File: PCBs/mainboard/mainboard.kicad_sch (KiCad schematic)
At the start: 26 parts, among them J1 USB_C_Receptacle_USB2.0_16P, SW1 SW_Push_Dual, SW2 SW_Push_Dual, U3 ESP32-S3-WROOM-1

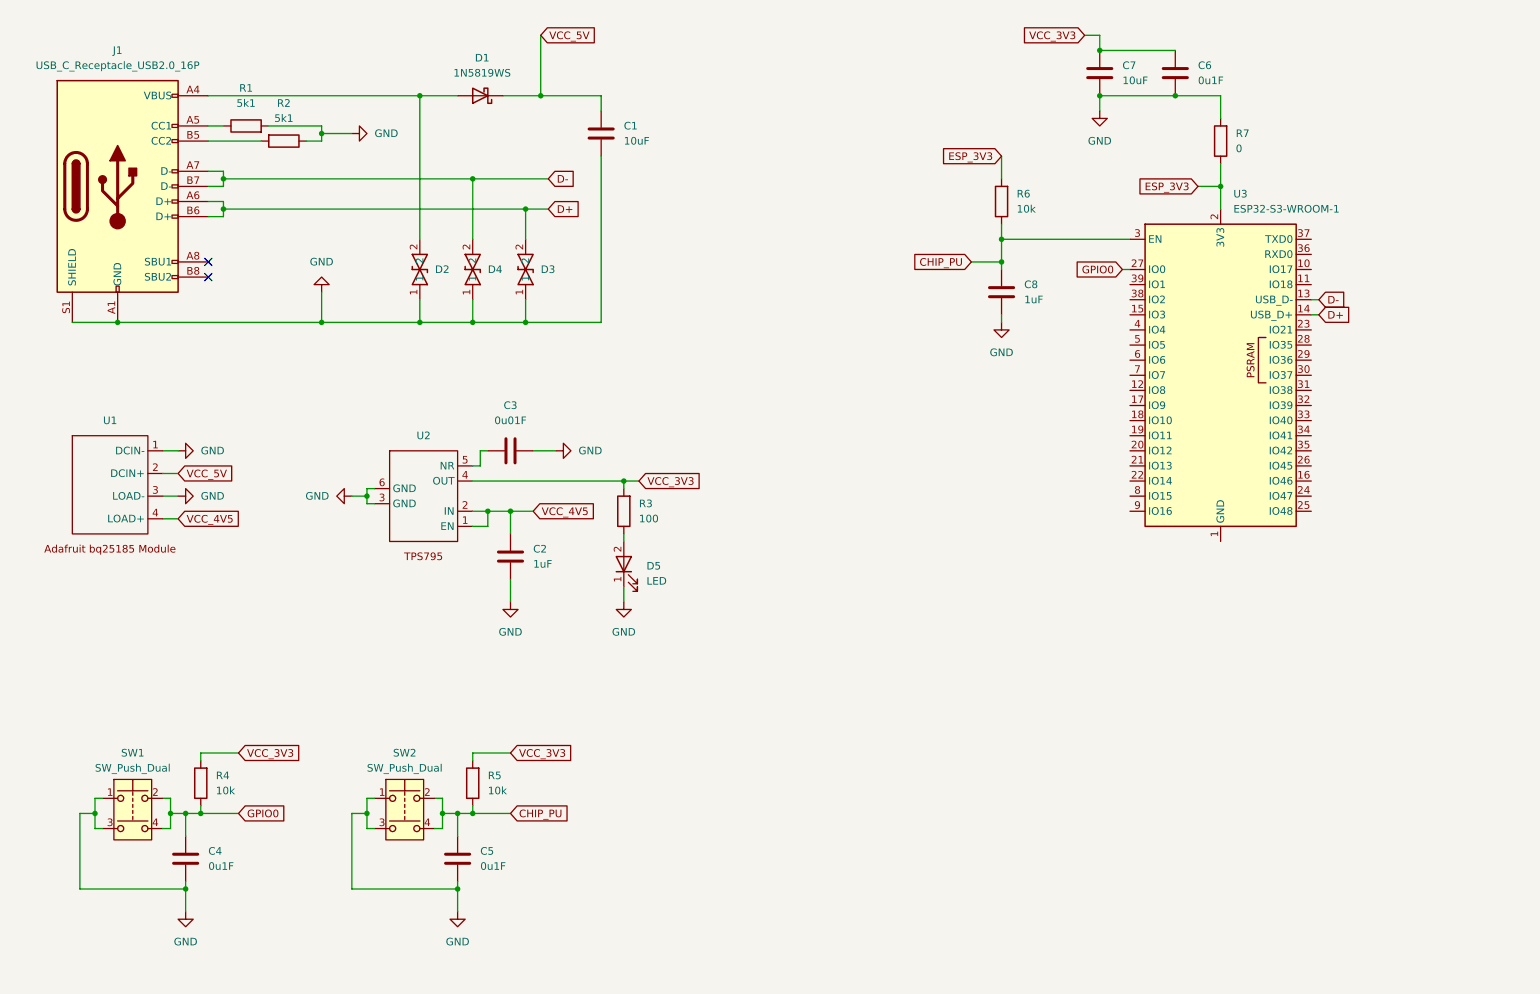
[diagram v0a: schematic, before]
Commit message: Fixed Display Code + Added Peripherals on Schematic
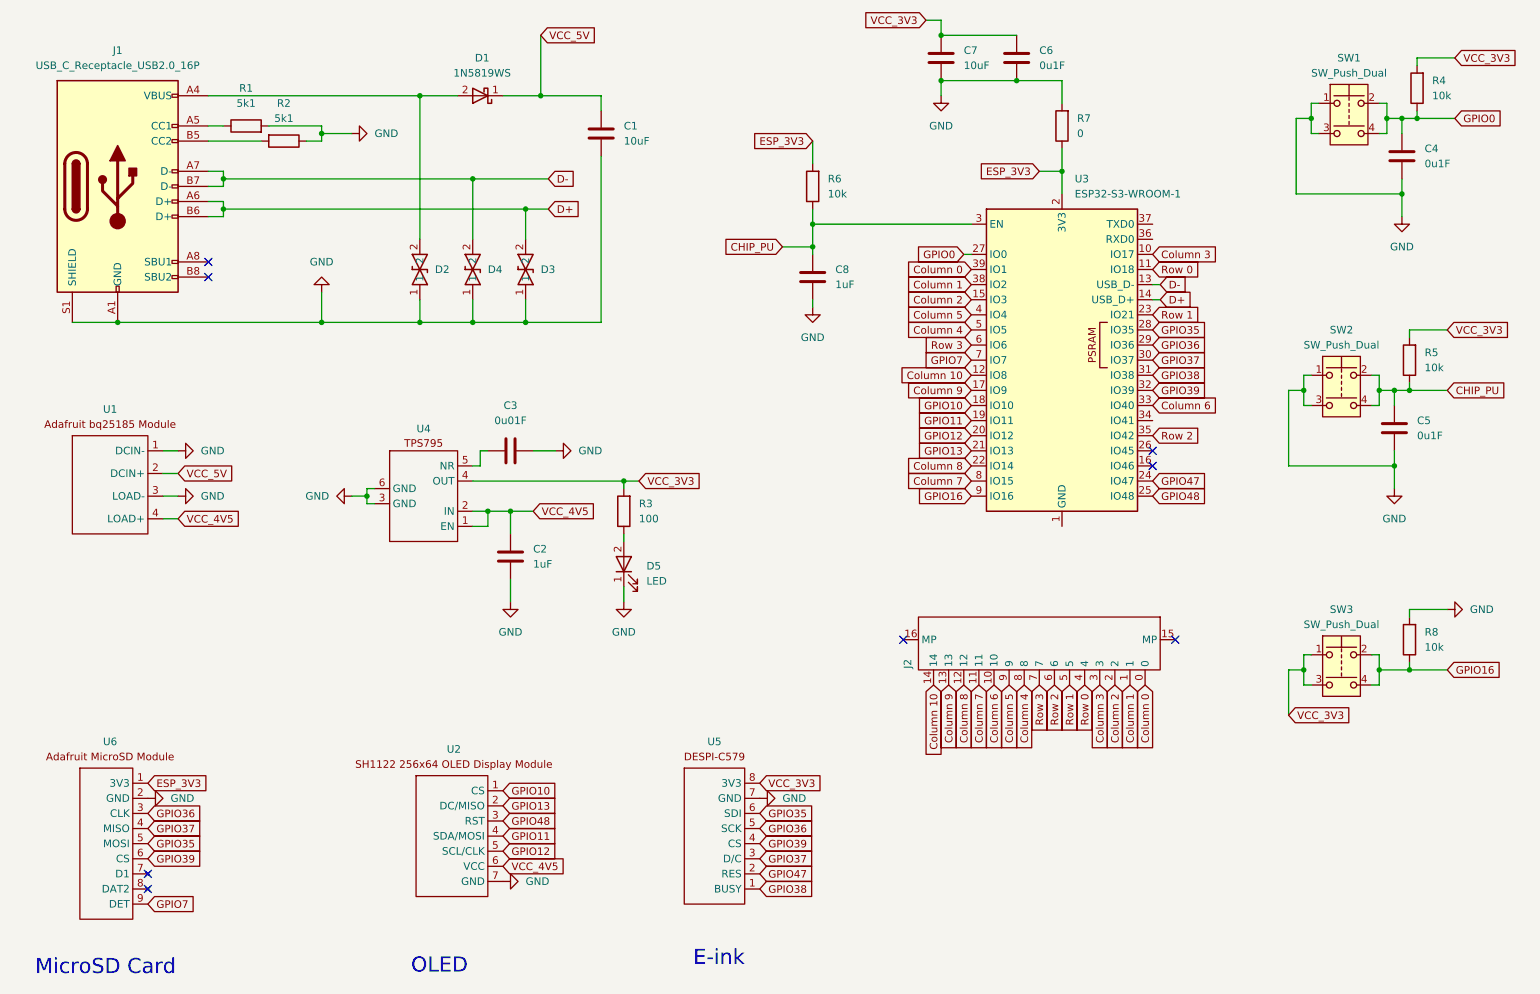
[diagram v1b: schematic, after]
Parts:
- removed U2: ~, symbol Custom:TPS795
- added J2: ~, Custom:FPC_15, symbol Custom:FPC-1.0FX-15PWCR-H20
- added R8: 10k, symbol Device:R
- added SW3: SW_Push_Dual, symbol Switch:SW_Push_Dual
- added U2: ~, symbol Custom:SH1122_256x64_OLED_Display_Module
- added U4: ~, symbol Custom:TPS795
- added U5: ~, symbol Custom:DESPI-C579
- added U6: ~, symbol Custom:Adafruit_MicroSD_Module
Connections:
- net ESP_3V3: now also U6.1 (3V3)
- net GND: now also R8.2, U2.7 (GND), U4.3 (GND), U4.6 (GND), U5.7 (GND), U6.2 (GND)
- net VCC_3V3: now also SW3.1, SW3.3, U4.4 (OUT), U5.8 (3V3)
- net VCC_4V5: now also U2.6 (VCC), U4.1 (EN), U4.2 (IN)
- net at C3.2: now also U4.5 (NR)
- net Column 3: now reaches U3.10 (IO17)
- net Column 3: now also J2.3
- net Row 0: now reaches U3.11 (IO18)
- net Row 0: now also J2.4
- net Column 10: now reaches U3.12 (IO8)
- net Column 10: now also J2.14
- net Column 2: now reaches U3.15 (IO3)
- net Column 2: now also J2.2
- net Column 9: now reaches U3.17 (IO9)
- net Column 9: now also J2.13
- net GPIO10: now reaches U3.18 (IO10)
- net GPIO10: now also U2.1 (CS)
- net GPIO11: now reaches U3.19 (IO11)
- net GPIO11: now also U2.4 (SDA/MOSI)
- net GPIO12: now reaches U3.20 (IO12)
- net GPIO12: now also U2.5 (SCL/CLK)
- net GPIO13: now reaches U3.21 (IO13)
- net GPIO13: now also U2.2 (DC/MISO)
- net Column 8: now reaches U3.22 (IO14)
- net Column 8: now also J2.12
- net Row 1: now reaches U3.23 (IO21)
- net Row 1: now also J2.5
- net GPIO47: now reaches U3.24 (IO47)
- net GPIO47: now also U5.2 (RES)
- net GPIO48: now reaches U3.25 (IO48)
- net GPIO48: now also U2.3 (RST)
- net GPIO35: now reaches U3.28 (IO35)
- net GPIO35: now also U5.6 (SDI), U6.5 (MOSI)
- net GPIO36: now reaches U3.29 (IO36)
- net GPIO36: now also U5.5 (SCK), U6.3 (CLK)
- net GPIO37: now reaches U3.30 (IO37)
- net GPIO37: now also U5.3 (D/C), U6.4 (MISO)
- net GPIO38: now reaches U3.31 (IO38)
- net GPIO38: now also U5.1 (BUSY)
- net GPIO39: now reaches U3.32 (IO39)
- net GPIO39: now also U5.4 (CS), U6.6 (CS)
- net Column 6: now reaches U3.33 (IO40)
- net Column 6: now also J2.10
- net Row 2: now reaches U3.35 (IO42)
- net Row 2: now also J2.6
- net Column 1: now reaches U3.38 (IO2)
- net Column 1: now also J2.1
- net Column 0: now reaches U3.39 (IO1)
- net Column 0: now also J2.0
- net Column 5: now reaches U3.4 (IO4)
- net Column 5: now also J2.9
- net Column 4: now reaches U3.5 (IO5)
- net Column 4: now also J2.8
- net Row 3: now reaches U3.6 (IO6)
- net Row 3: now also J2.7
- net GPIO7: now reaches U3.7 (IO7)
- net GPIO7: now also U6.9 (DET)
- net Column 7: now reaches U3.8 (IO15)
- net Column 7: now also J2.11
- net GPIO16: now reaches U3.9 (IO16)
- net GPIO16: now also R8.1, SW3.2, SW3.4
- no-connect marks 2 -> 8
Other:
- note added: "E-ink"
- note added: "MicroSD Card"
- note added: "OLED"
- moved on the sheet: C4, C5, C6, C7, C8, R4, R5, R6, R7, SW1, SW2, U3

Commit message: CAD Mockup and Footprint Design
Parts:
- C1, C2, C3, C4, C5, C6, C7, C8: footprint (none) -> Capacitor_SMD:C_0805_2012Metric
- D1: footprint Diode_SMD:D_SOD-323 -> Custom:1N5819HW-7-F
- D2, D3, D4: footprint (none) -> Custom:LESD5D5
- D5: footprint (none) -> Custom:KT-0805G
- J1: footprint (none) -> Custom:USB_C_Receptacle_16P
- R1, R2, R3, R4, R5, R6, R7, R8: footprint (none) -> Resistor_SMD:R_0805_2012Metric
- SW1, SW2, SW3: footprint (none) -> Custom:B3F-1000
- U4: footprint (none) -> Custom:TPS795
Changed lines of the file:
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@@
 			)
 		)
-		(property "Footprint" ""
+		(property "Footprint" "Resistor_SMD:R_0805_2012Metric"
 			(at 123.698 105.41 90)
 			(effects
@@
 			)
 		)
-		(property "Footprint" ""
+		(property "Footprint" "Resistor_SMD:R_0805_2012Metric"
 			(at 255.778 127 90)
 			(effects
@@
 			)
 		)
-		(property "Footprint" ""
+		(property "Footprint" "Capacitor_SMD:C_0805_2012Metric"
 			(at 103.8352 116.84 0)
 			(effects
@@
 			)
 		)
-		(property "Footprint" ""
+		(property "Footprint" "Resistor_SMD:R_0805_2012Metric"
 			(at 197.358 40.64 90)
 			(effects
@@
 			)
 		)
-		(property "Footprint" "Diode_SMD:D_SOD-323"
+		(property "Footprint" "Custom:1N5819HW-7-F"
 			(at 97.79 31.115 0)
 			(effects
@@
 			)
 		)
-		(property "Footprint" ""
+		(property "Footprint" "Custom:B3F-1000"
 			(at 243.84 31.75 0)
 			(effects
@@
 			)
 		)
-		(property "Footprint" ""
+		(property "Footprint" "Capacitor_SMD:C_0805_2012Metric"
 			(at 176.2252 33.02 0)
 			(effects
@@
 			)
 		)
-		(property "Footprint" ""
+		(property "Footprint" "Resistor_SMD:R_0805_2012Metric"
 			(at 257.048 34.29 90)
 			(effects
@@
 			)
 		)
-		(property "Footprint" ""
+		(property "Footprint" "Custom:KT-0805G"
 			(at 121.92 114.3 0)
 			(effects
@@
 			)
 		)
-		(property "Footprint" ""
+		(property "Footprint" "Custom:B3F-1000"
 			(at 242.57 124.46 0)
 			(effects
@@
 			)
 		)
-		(property "Footprint" ""
+		(property "Footprint" "Capacitor_SMD:C_0805_2012Metric"
 			(at 188.9252 33.02 0)
 			(effects
@@
 			)
 		)
-		(property "Footprint" ""
+		(property "Footprint" "Custom:B3F-1000"
 			(at 242.57 77.47 0)
 			(effects
@@
 			)
 		)
-		(property "Footprint" ""
+		(property "Footprint" "Resistor_SMD:R_0805_2012Metric"
 			(at 58.42 42.418 90)
 			(effects
@@
 			)
 		)
-		(property "Footprint" ""
+		(property "Footprint" "Custom:LESD5D5"
 			(at 87.63 64.77 0)
 			(effects
@@
 			)
 		)
-		(property "Footprint" ""
+		(property "Footprint" "Resistor_SMD:R_0805_2012Metric"
 			(at 64.77 41.402 90)
 			(effects
@@
 			)
 		)
-		(property "Footprint" ""
+		(property "Footprint" "Capacitor_SMD:C_0805_2012Metric"
 			(at 99.06 96.2152 0)
 			(effects
@@
 			)
 		)
-		(property "Footprint" ""
+		(property "Footprint" "Resistor_SMD:R_0805_2012Metric"
 			(at 155.448 50.8 90)
 			(effects
@@
 			)
 		)
-		(property "Footprint" ""
+		(property "Footprint" "Custom:LESD5D5"
 			(at 96.52 64.77 0)
 			(effects
@@
 			)
 		)
-		(property "Footprint" ""
+		(property "Footprint" "Custom:USB_C_Receptacle_16P"
 			(at 40.64 50.8 0)
 			(effects
@@
 			)
 		)
-		(property "Footprint" ""
+		(property "Footprint" "Capacitor_SMD:C_0805_2012Metric"
 			(at 154.6352 69.85 0)
 			(effects
@@
 			)
 		)
-		(property "Footprint" ""
+		(property "Footprint" "Resistor_SMD:R_0805_2012Metric"
 			(at 255.778 80.01 90)
 			(effects
@@
 			)
 		)
-		(property "Footprint" ""
+		(property "Footprint" "Capacitor_SMD:C_0805_2012Metric"
 			(at 252.4252 95.25 0)
 			(effects
@@
 			)
 		)
-		(property "Footprint" ""
+		(property "Footprint" "Custom:TPS795"
 			(at 88.265 102.87 0)
 			(effects
@@
 			)
 		)
-		(property "Footprint" ""
+		(property "Footprint" "Capacitor_SMD:C_0805_2012Metric"
 			(at 253.6952 49.53 0)
 			(effects
@@
 			)
 		)
-		(property "Footprint" ""
+		(property "Footprint" "Custom:LESD5D5"
 			(at 105.41 64.77 0)
 			(effects
@@
 			)
 		)
-		(property "Footprint" ""
+		(property "Footprint" "Capacitor_SMD:C_0805_2012Metric"
 			(at 119.0752 45.72 0)
 			(effects

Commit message: Layouting + Deep Sleep Tests
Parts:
- U1: footprint (none) -> Custom:Adafruit bq25185 Module
- U2: footprint (none) -> Custom:SH1122 256x64 OLED Display Module
- U5: footprint (none) -> Custom:DESPI-C579
- U6: footprint (none) -> Custom:Adafruit MicroSD Module
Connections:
- net Column 3: now also J2.7; no longer J2.3
- net GND: now also U3.1 (GND), U3.40 (GND), U3.41 (GND)
- net Row 0: now also J2.3; no longer J2.4
- net Row 1: now also J2.4; no longer J2.5
- net Row 2: now also J2.5; no longer J2.6
- net Row 3: now also J2.6; no longer J2.7
- no-connect marks 8 -> 11

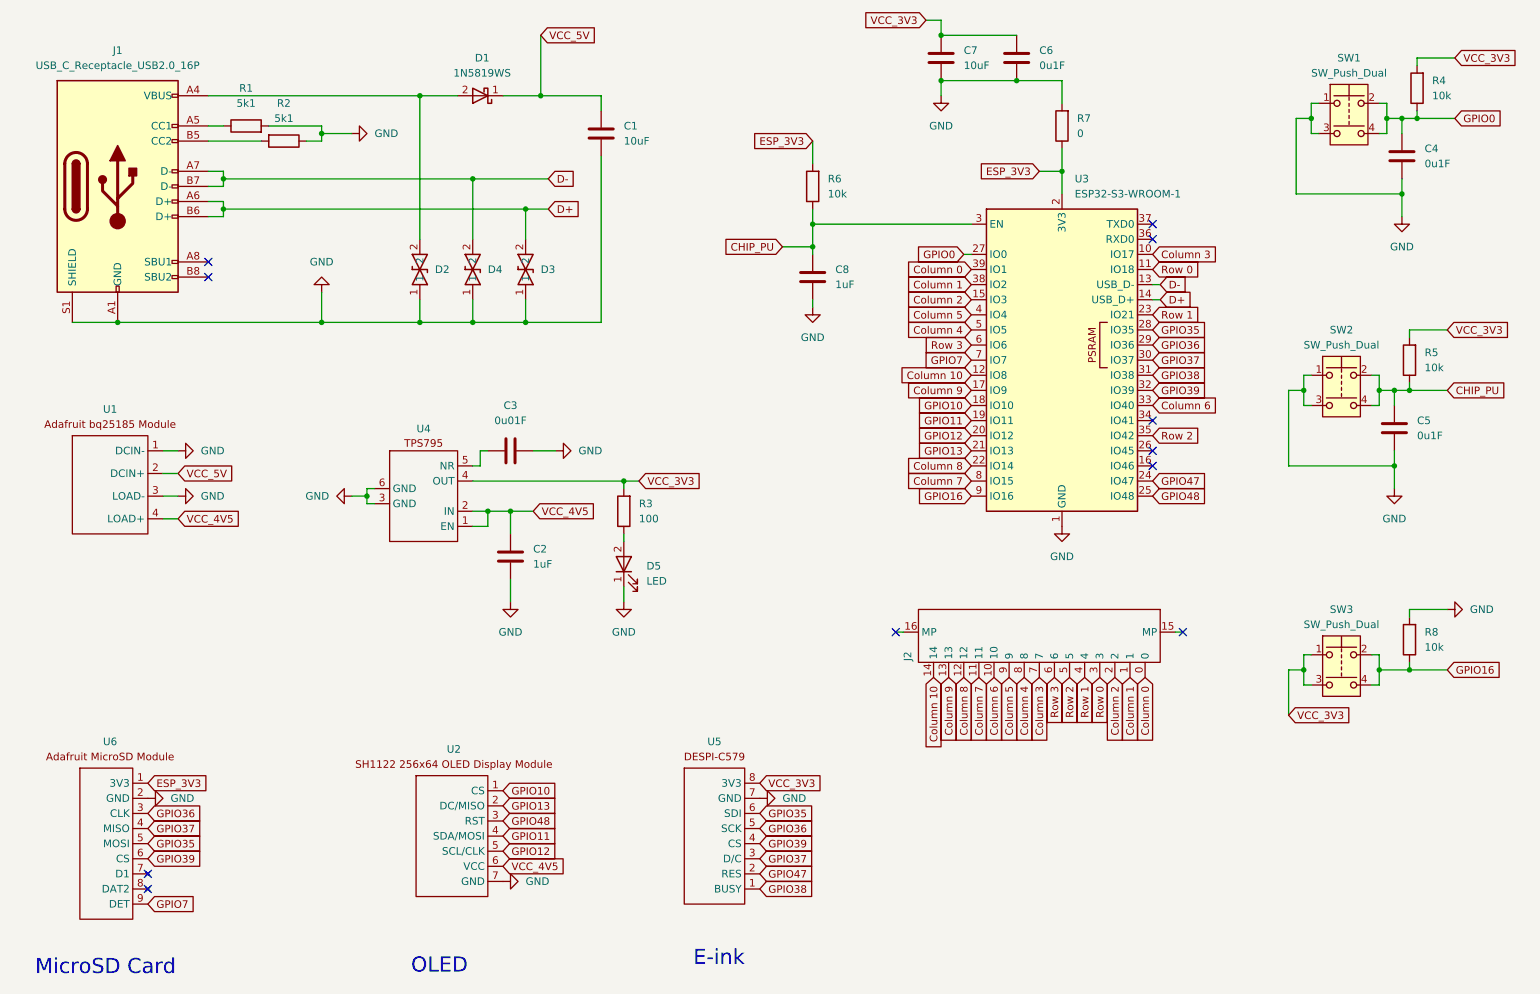
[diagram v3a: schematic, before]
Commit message: Routed peripherals
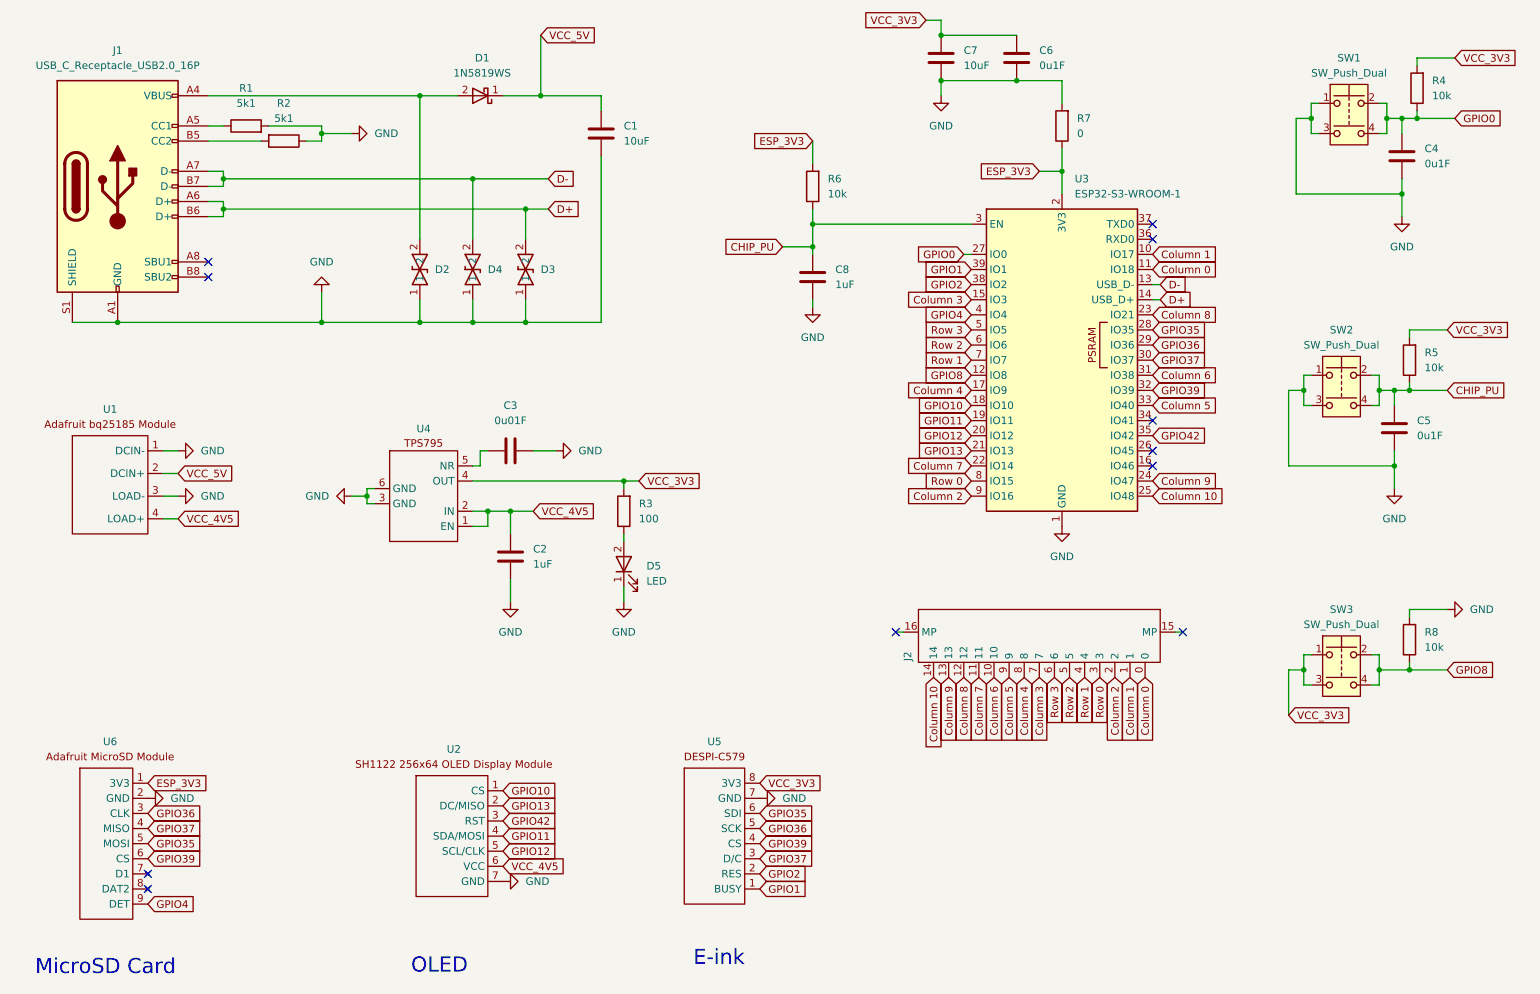
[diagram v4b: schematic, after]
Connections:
- net Column 0: now also U3.11 (IO18); no longer U3.39 (IO1)
- net Column 1: now also U3.10 (IO17); no longer U3.38 (IO2)
- net Column 10: now also U3.25 (IO48); no longer U3.12 (IO8)
- net Column 2: now also U3.9 (IO16); no longer U3.15 (IO3)
- net Column 3: now also U3.15 (IO3); no longer U3.10 (IO17)
- net Column 4: now also U3.17 (IO9); no longer U3.5 (IO5)
- net Column 5: now also U3.33 (IO40); no longer U3.4 (IO4)
- net Column 6: now also U3.31 (IO38); no longer U3.33 (IO40)
- net Column 7: now also U3.22 (IO14); no longer U3.8 (IO15)
- net Column 8: now also U3.23 (IO21); no longer U3.22 (IO14)
- net Column 9: now also U3.24 (IO47); no longer U3.17 (IO9)
- net Row 0: now also U3.8 (IO15); no longer U3.11 (IO18)
- net Row 1: now also U3.7 (IO7); no longer U3.23 (IO21)
- net Row 2: now also U3.6 (IO6); no longer U3.35 (IO42)
- net Row 3: now also U3.5 (IO5); no longer U3.6 (IO6)
- net GPIO16 renamed GPIO8
- net GPIO8: now also U3.12 (IO8); no longer U3.9 (IO16)
- net GPIO38 renamed GPIO1
- net GPIO1: now also U3.39 (IO1); no longer U3.31 (IO38)
- net GPIO47 renamed GPIO2
- net GPIO2: now also U3.38 (IO2); no longer U3.24 (IO47)
- net GPIO48 renamed GPIO42
- net GPIO42: now also U3.35 (IO42); no longer U3.25 (IO48)
- net GPIO7 renamed GPIO4
- net GPIO4: now also U3.4 (IO4); no longer U3.7 (IO7)
